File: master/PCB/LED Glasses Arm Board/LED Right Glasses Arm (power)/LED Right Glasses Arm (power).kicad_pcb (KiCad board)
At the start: 2 copper layers, 0 parts

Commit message: Started on the PCB
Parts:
- added C1: 20u, Capacitor_SMD:C_0603_1608Metric, F.Cu at (189.2, 52.5)
- added C2: 0.1u, Capacitor_SMD:C_0603_1608Metric, F.Cu at (186.6, 53.9)
- added C3: 10p, Capacitor_SMD:C_0603_1608Metric, F.Cu at (188.4, 50.1)
- added C4: 66u, Capacitor_SMD:C_0603_1608Metric, F.Cu at (184.0, 54.3)
- added D1: D_Zener_Small, Diode_SMD:D_0603_1608Metric, F.Cu at (181.4, 55.7)
- added D2: LED, LED_SMD:LED_0603_1608Metric, F.Cu at (179.6, 55.3)
- added D3: LED, LED_SMD:LED_0603_1608Metric, F.Cu at (185.8, 50.6)
- added L1: 1u, Inductor_SMD:L_Coilcraft_XxL4020, F.Cu at (182.9, 94.0)
- added Q1: TP0610T, Package_TO_SOT_SMD:SOT-23, F.Cu at (146.6, 93.9)
- added R1: R_Small_US, Resistor_SMD:R_0603_1608Metric, F.Cu at (191.0, 53.4)
- added R2: 2k2, Resistor_SMD:R_0603_1608Metric, F.Cu at (193.6, 52.0)
- added R3: 1M, Resistor_SMD:R_0603_1608Metric, F.Cu at (190.1, 54.8)
- added R4: 111k, Resistor_SMD:R_0603_1608Metric, F.Cu at (184.9, 52.9)
- added R5: 1MOhm, Resistor_SMD:R_0603_1608Metric, F.Cu at (192.8, 49.7)
- added R6: 2k2, Resistor_SMD:R_0603_1608Metric, F.Cu at (187.5, 56.2)
- added SW1: SW_SPST, Button_Switch_SMD:SW_SPST_FSMSM, F.Cu at (200.7, 94.0)
- added U1: TPS63060, Package_SON:Texas_S-PWSON-N10_ThermalVias, F.Cu at (174.5, 94.0)

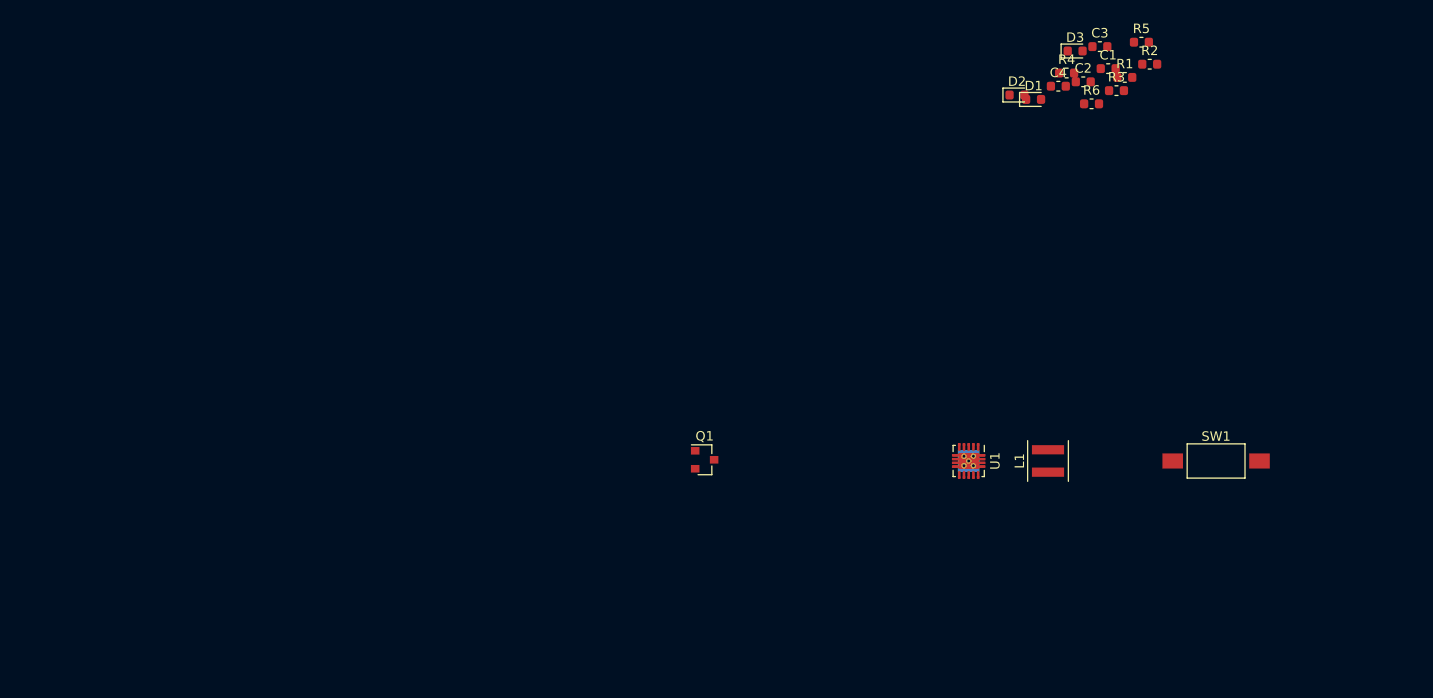
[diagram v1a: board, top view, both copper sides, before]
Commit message: Finalising sch and board layout
Added in JST connector for battery pack and pin connectors for the glasses side. Prelim board layout
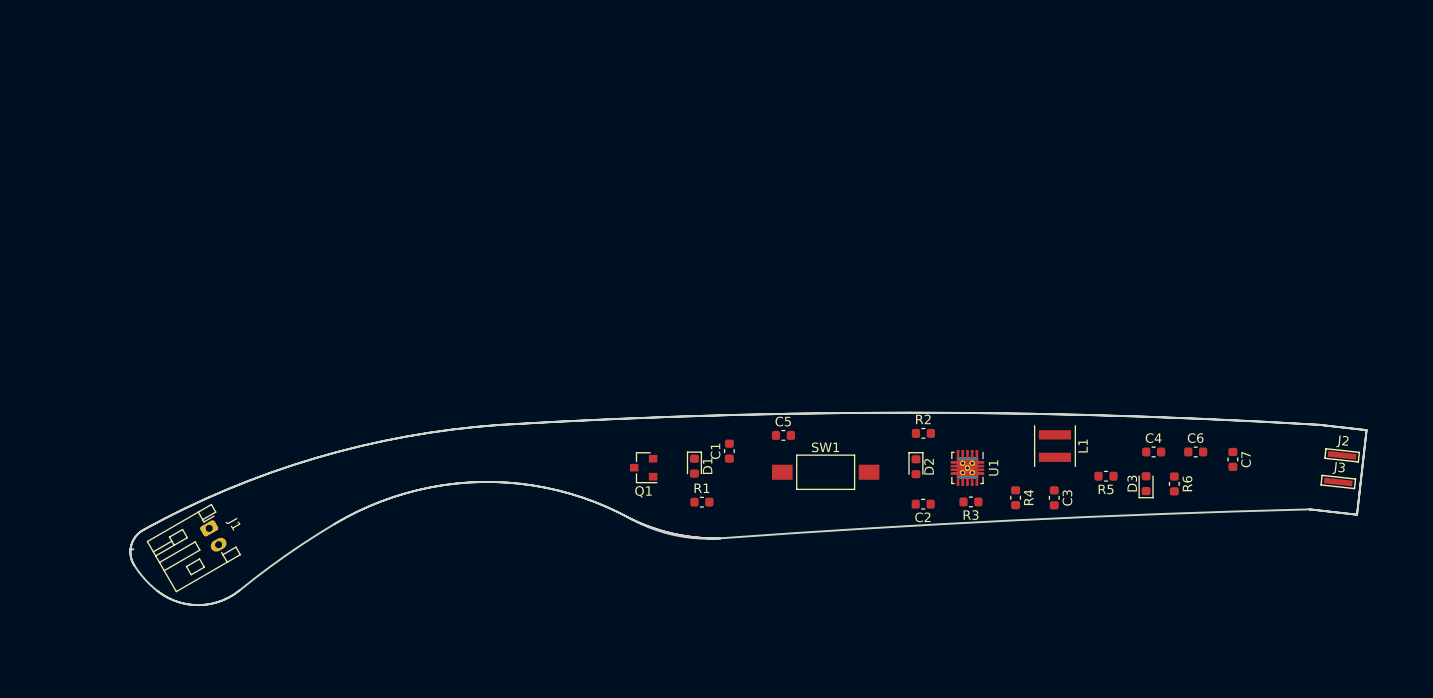
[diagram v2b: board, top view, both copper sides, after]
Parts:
- added C5: 10uF, Capacitor_SMD:C_0603_1608Metric, F.Cu at (154.9, 91.3)
- added C6: 22uF, Capacitor_SMD:C_0603_1608Metric, F.Cu at (198.5, 93.0)
- added C7: 22uF, Capacitor_SMD:C_0603_1608Metric, F.Cu at (202.4, 93.8)
- added J1: Conn_01x02_Male, Connector_JST:JST_PH_S2B-PH-K_1x02_P2.00mm_Horizontal, F.Cu at (94.1, 101.1)
- added J2: Conn_01x01_Male, Connector_PinHeader_1.00mm:PinHeader_1x01_P1.00mm_Vertical_SMD_CUSTOM, F.Cu at (213.8, 95.4)
- added J3: Conn_01x01_Male, Connector_PinHeader_1.00mm:PinHeader_1x01_P1.00mm_Vertical_SMD_CUSTOM, F.Cu at (213.4, 98.2)
- C1: value 20u -> 10uF
- C3: value 10p -> 10pF
- C4: value 66u -> 22uF
- moved R1 63.4 mm to (146.3, 98.3)
- moved C1 56.9 mm to (149.2, 92.9), turned to 90 degrees
- moved D1 52.8 mm to (145.5, 94.5), turned to 270 degrees
- moved C3 48.0 mm to (183.5, 97.9), turned to 270 degrees
- moved C2 47.8 mm to (169.7, 98.6), turned to 180 degrees
- moved D3 46.4 mm to (193.3, 96.4), turned to 90 degrees
- moved R3 46.2 mm to (174.7, 98.3), turned to 180 degrees
- moved R5 46.1 mm to (189.0, 95.6), turned to 180 degrees
- moved R2 45.8 mm to (169.7, 91.1)
- moved R4 45.3 mm to (179.5, 97.9), turned to 270 degrees
- moved SW1 41.3 mm to (159.4, 95.2)
- moved R6 41.1 mm to (196.2, 96.4), turned to 270 degrees
- moved D2 40.7 mm to (168.9, 94.6), turned to 270 degrees
- moved C4 40.0 mm to (194.1, 93.0)
- moved Q1 6.51 mm to (140.1, 94.7), turned to 180 degrees
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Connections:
- net /VOUT renamed /VOUT_5V
- C1 pad 2: GND -> Net-(C1-Pad2)
- C4 pad 2: GND -> Net-(C4-Pad2)
- Q1 pad 3: /VIN -> /VIN_2.5-12V
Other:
- board outline added: 130.8 x 20.4 mm

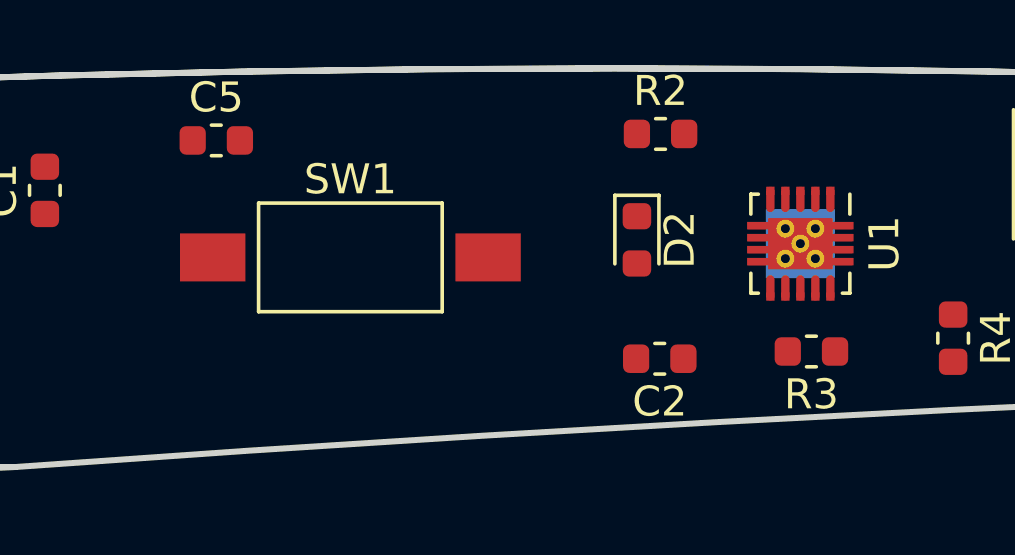
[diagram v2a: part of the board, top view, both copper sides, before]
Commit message: sch revs
added 1000uF cap, slide switch and changed caps to parallel. need to change mosfet and do footprint for cap
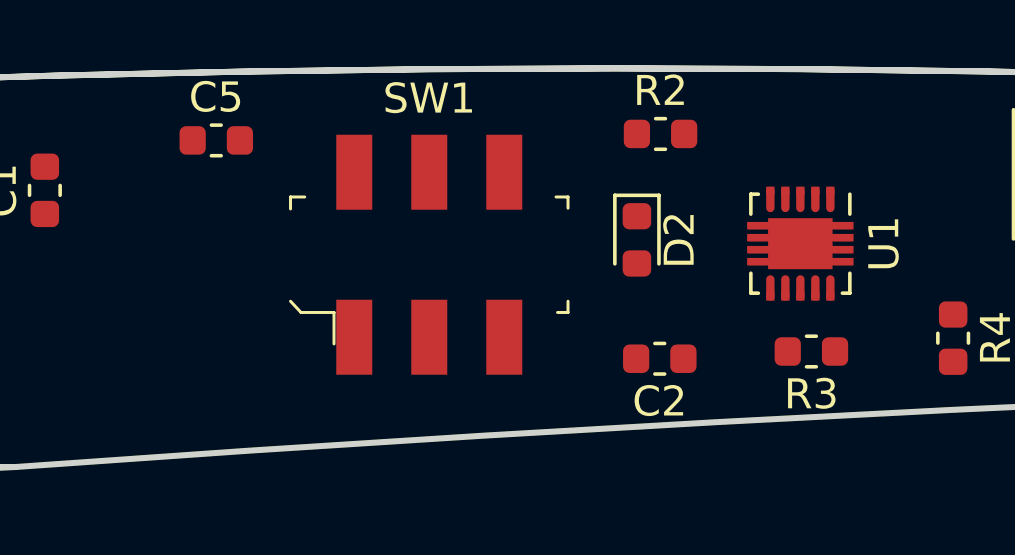
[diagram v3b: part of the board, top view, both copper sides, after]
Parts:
- SW1: footprint Button_Switch_SMD:SW_SPST_FSMSM -> digikey-footprints:Switch_Slide_JS202011SCQN
- U1: footprint Package_SON:Texas_S-PWSON-N10_ThermalVias -> Package_SON:Texas_S-PWSON-N10
- moved SW1 2.63 mm to (162.0, 95.1)
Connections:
- C1 pad 2: Net-(C1-Pad2) -> GND
- C4 pad 2: Net-(C4-Pad2) -> GND
- C5 pad 1: Net-(C1-Pad2) -> Net-(C1-Pad1)
- C6 pad 1: Net-(C4-Pad2) -> /VOUT_5V
- C6 pad 2: Net-(C6-Pad2) -> GND
- C7 pad 1: Net-(C6-Pad2) -> /VOUT_5V

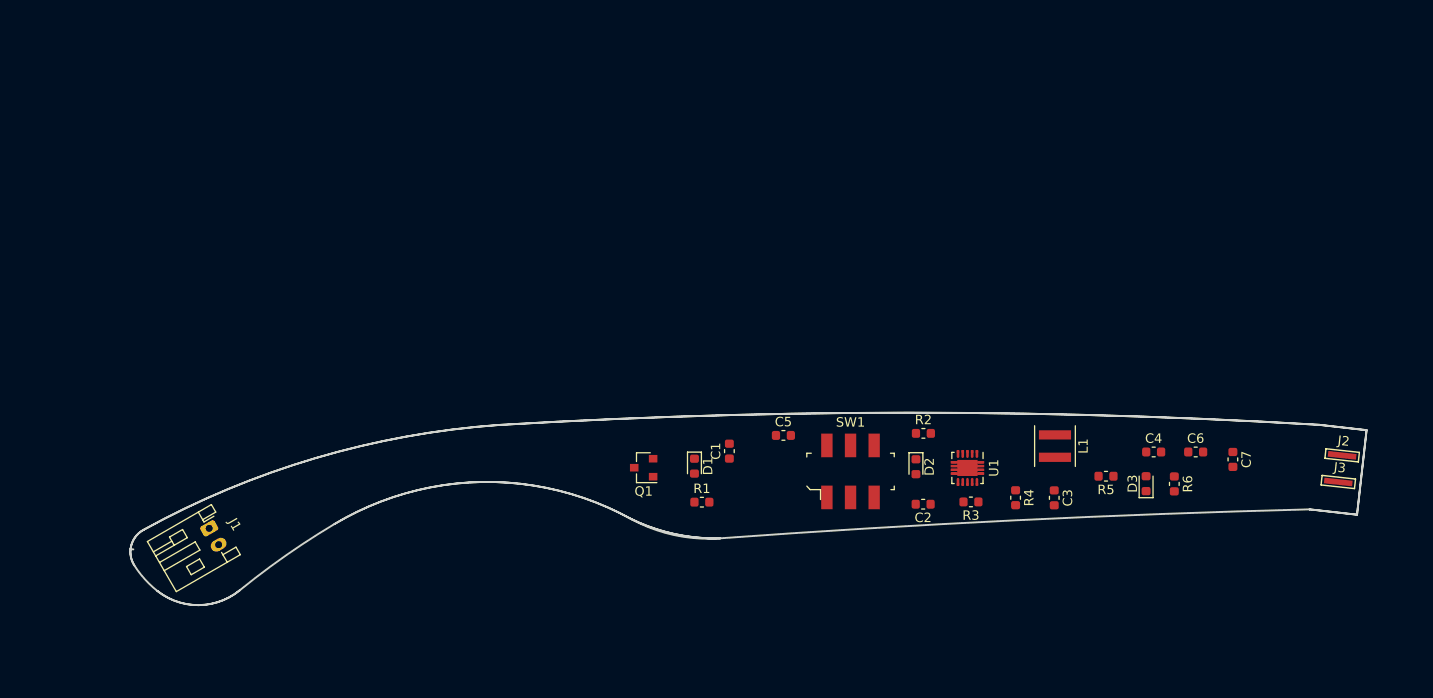
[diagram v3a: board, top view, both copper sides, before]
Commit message: PCB update
Changed mosfet, started to route signals
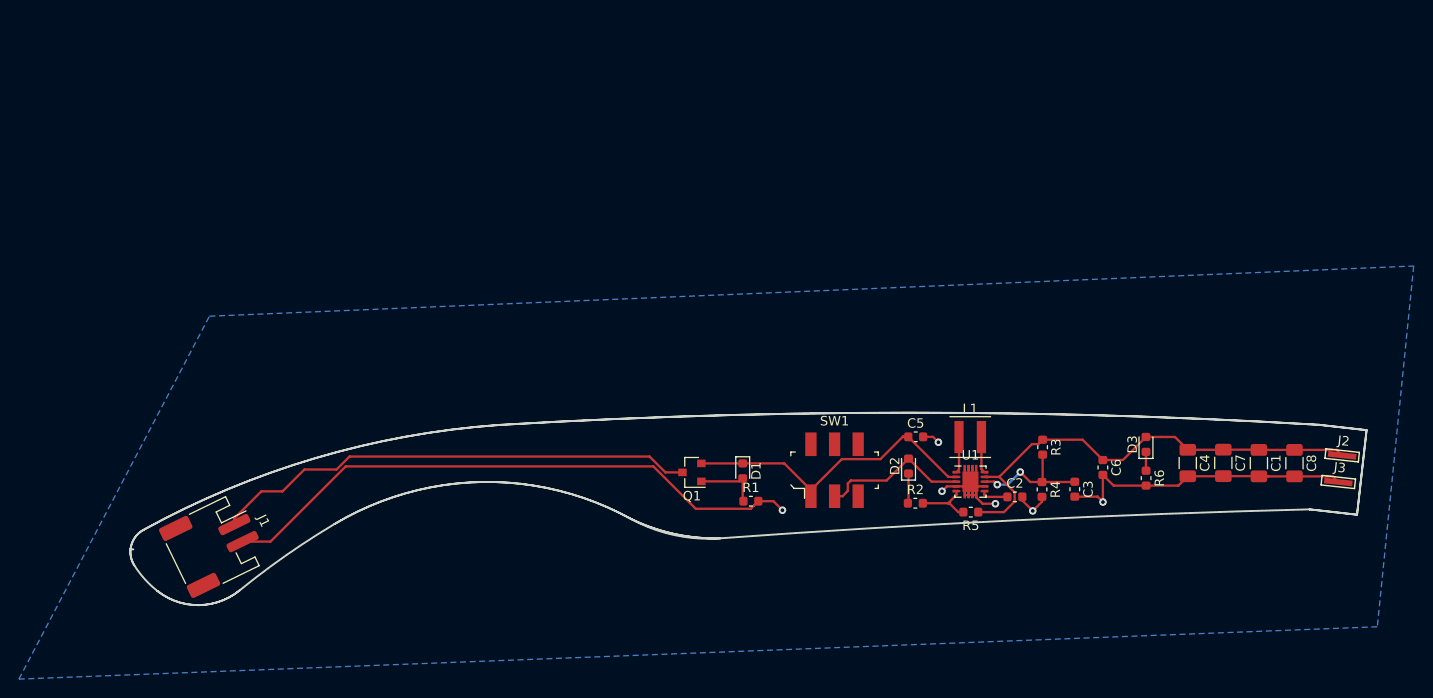
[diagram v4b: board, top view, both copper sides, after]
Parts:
- added C8: 220uF, Capacitor_SMD:C_1206_3216Metric, F.Cu at (209.0, 94.2)
- C1: value 10uF -> 220uF; footprint Capacitor_SMD:C_0603_1608Metric -> Capacitor_SMD:C_1206_3216Metric
- C4, C7: value 22uF -> 220uF; footprint Capacitor_SMD:C_0603_1608Metric -> Capacitor_SMD:C_1206_3216Metric
- C5: value 10uF -> 20uF
- C6: value 22uF -> 66uF
- J1: footprint Connector_JST:JST_PH_S2B-PH-K_1x02_P2.00mm_Horizontal -> Connector_JST:JST_PH_S2B-PH-SM4-TB_1x02-1MP_P2.00mm_Horizontal
- L1: value 1u -> 1uF
- moved C1 56.0 mm to (205.2, 94.2), turned to 270 degrees
- moved R5 14.8 mm to (174.7, 99.4)
- moved C5 14.0 mm to (168.9, 91.4)
- moved C6 9.95 mm to (188.7, 94.7), turned to 270 degrees
- moved C2 9.73 mm to (179.4, 97.8), turned to 0 degrees
- moved R3 9.54 mm to (182.3, 92.5), turned to 270 degrees
- moved L1 9.02 mm to (174.7, 91.5), turned to 0 degrees
- moved R2 7.44 mm to (168.8, 98.5)
- moved R1 5.18 mm to (151.4, 98.2)
- moved D1 5.13 mm to (150.6, 95.0)
- moved Q1 5.13 mm to (145.2, 95.2)
- moved D3 4.15 mm to (193.2, 92.2)
- moved C4 3.79 mm to (197.7, 94.2), turned to 270 degrees
- moved R6 3.05 mm to (193.3, 95.8)
- moved R4 2.93 mm to (182.2, 97.0)
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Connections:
- C1 pad 1: Net-(C1-Pad1) -> /VOUT_5V
- C5 pad 1: Net-(C1-Pad1) -> Net-(C5-Pad1)
- D1 pad 1: Net-(C1-Pad1) -> Net-(C5-Pad1)
- Q1 pad 2: Net-(C1-Pad1) -> Net-(C5-Pad1)
- SW1 pad 1: Net-(C1-Pad1) -> Net-(C5-Pad1)
- U1 pad 2: Net-(C1-Pad1) -> Net-(C5-Pad1)
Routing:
- net GND: track 0.00 -> 109.7 mm, vias 0 -> 6
- net /VIN_2.5-12V: track 0.00 -> 51.5 mm
- net /VOUT_5V: track 0.00 -> 49.8 mm
- net Net-(C5-Pad1): track 0.00 -> 32.9 mm
- net Net-(D2-Pad2): track 0.00 -> 16.0 mm
- net Net-(C3-Pad1): track 0.00 -> 13.3 mm, vias 0 -> 2
- net Net-(D1-Pad2): track 0.00 -> 6.96 mm
- net /PG: track 0.00 -> 6.34 mm
- net Net-(L1-Pad2): track 0.00 -> 3.84 mm
- net Net-(L1-Pad1): track 0.00 -> 3.82 mm
- net Net-(D2-Pad1): track 0.00 -> 3.18 mm
- net Net-(C2-Pad1): track 0.00 -> 2.92 mm
- net Net-(D3-Pad1): track 0.00 -> 2.00 mm
- added copper zone on B.Cu, net GND

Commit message: added parts for caps
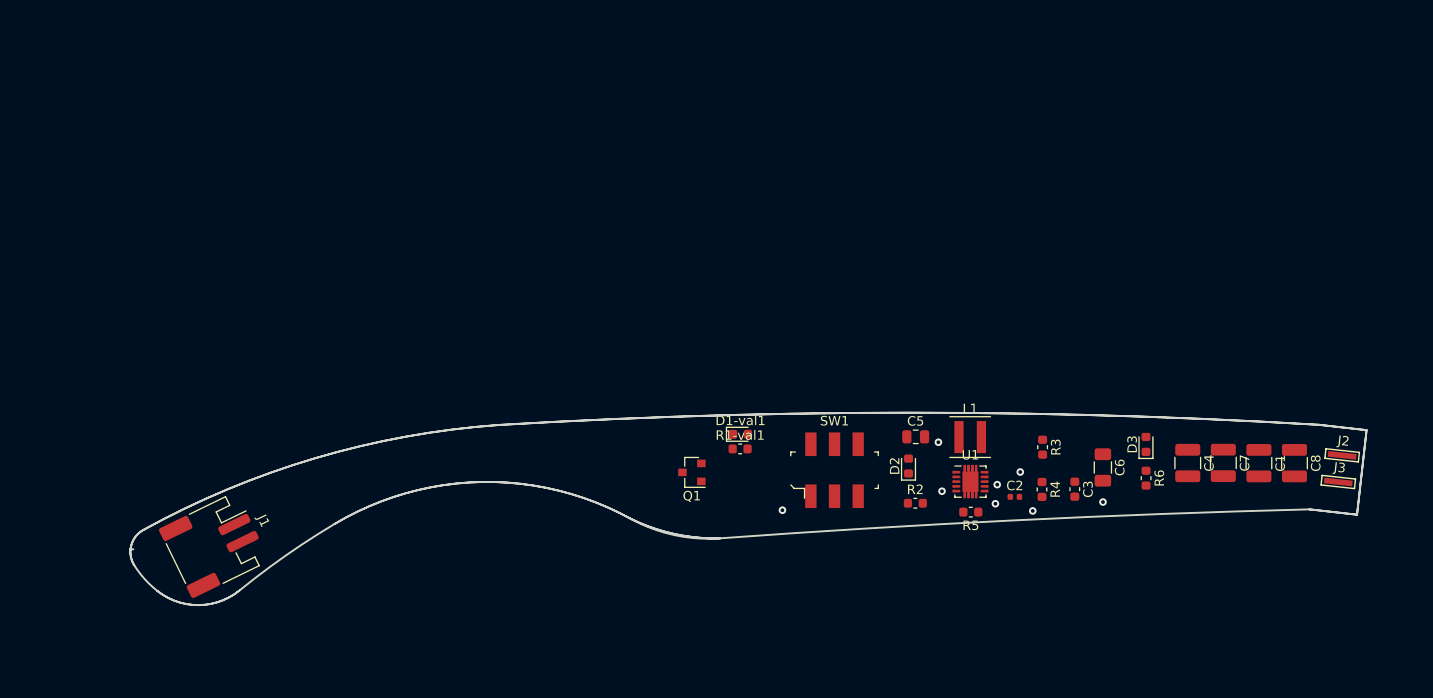
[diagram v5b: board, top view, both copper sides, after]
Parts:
- removed D1: D_Zener_Small, Diode_SMD:D_0603_1608Metric
- removed R1: R_Small_US, Resistor_SMD:R_0603_1608Metric
- added D1-val1: D_Zener_Small, Diode_SMD:D_0603_1608Metric, F.Cu at (150.4, 91.2)
- added R1-val1: R_Small_US, Resistor_SMD:R_0603_1608Metric, F.Cu at (150.3, 92.7)
- C1, C4, C7, C8: footprint Capacitor_SMD:C_1206_3216Metric -> Capacitor_SMD:C_1210_3225Metric
- C2: footprint Capacitor_SMD:C_0603_1608Metric -> Capacitor_SMD:C_0402_1005Metric
- C5: value 20uF -> 22uF; footprint Capacitor_SMD:C_0603_1608Metric -> Capacitor_SMD:C_0805_2012Metric
- C6: value 66uF -> 68uF; footprint Capacitor_SMD:C_0603_1608Metric -> Capacitor_SMD:C_1206_3216Metric
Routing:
- net GND: track 109.7 -> 0.00 mm
- net /VIN_2.5-12V: track 51.5 -> 0.00 mm
- net /VOUT_5V: track 49.8 -> 0.00 mm
- net Net-(C5-Pad1): track 32.9 -> 0.00 mm
- net Net-(D2-Pad2): track 16.0 -> 0.00 mm
- net Net-(C3-Pad1): track 13.3 -> 0.00 mm
- net Net-(D1-val1-Pad2): track 6.96 -> 0.00 mm
- net /PG: track 6.34 -> 0.00 mm
- net Net-(L1-Pad2): track 3.84 -> 0.00 mm
- net Net-(L1-Pad1): track 3.82 -> 0.00 mm
- net Net-(D2-Pad1): track 3.18 -> 0.00 mm
- net Net-(C2-Pad1): track 2.92 -> 0.00 mm
- net Net-(D3-Pad1): track 2.00 -> 0.00 mm
- removed copper zone on B.Cu, net GND
